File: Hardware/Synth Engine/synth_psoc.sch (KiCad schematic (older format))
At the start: 0 parts

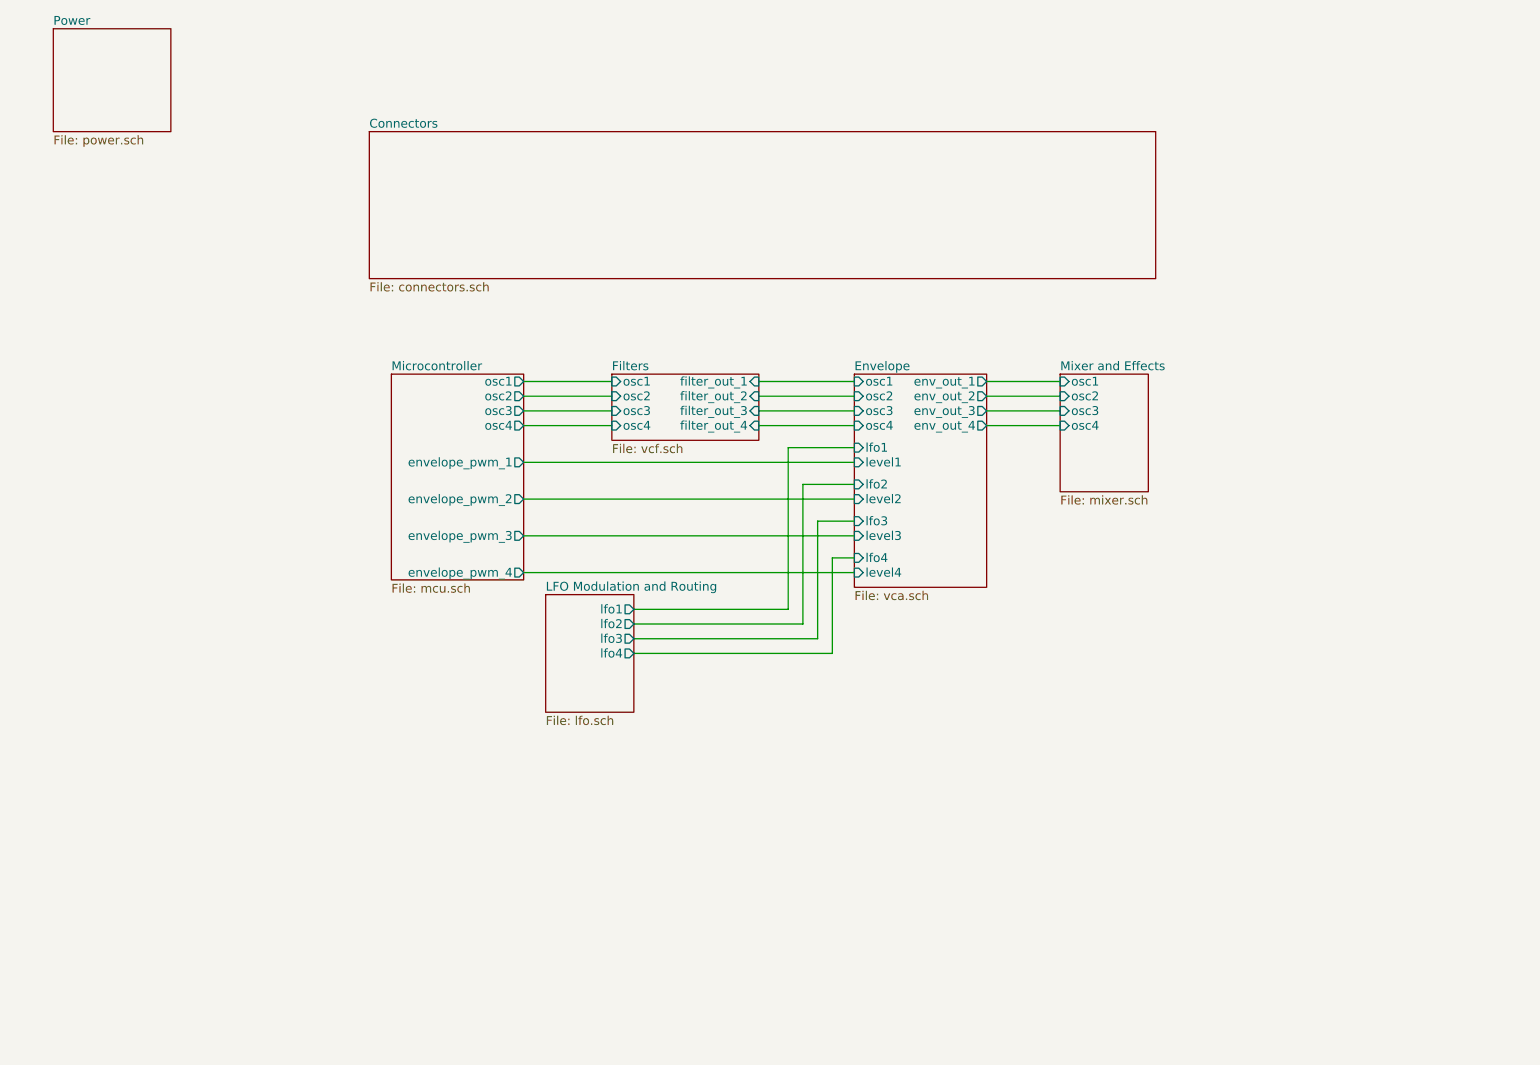
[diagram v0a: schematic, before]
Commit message: connect control board to main synth schem pages
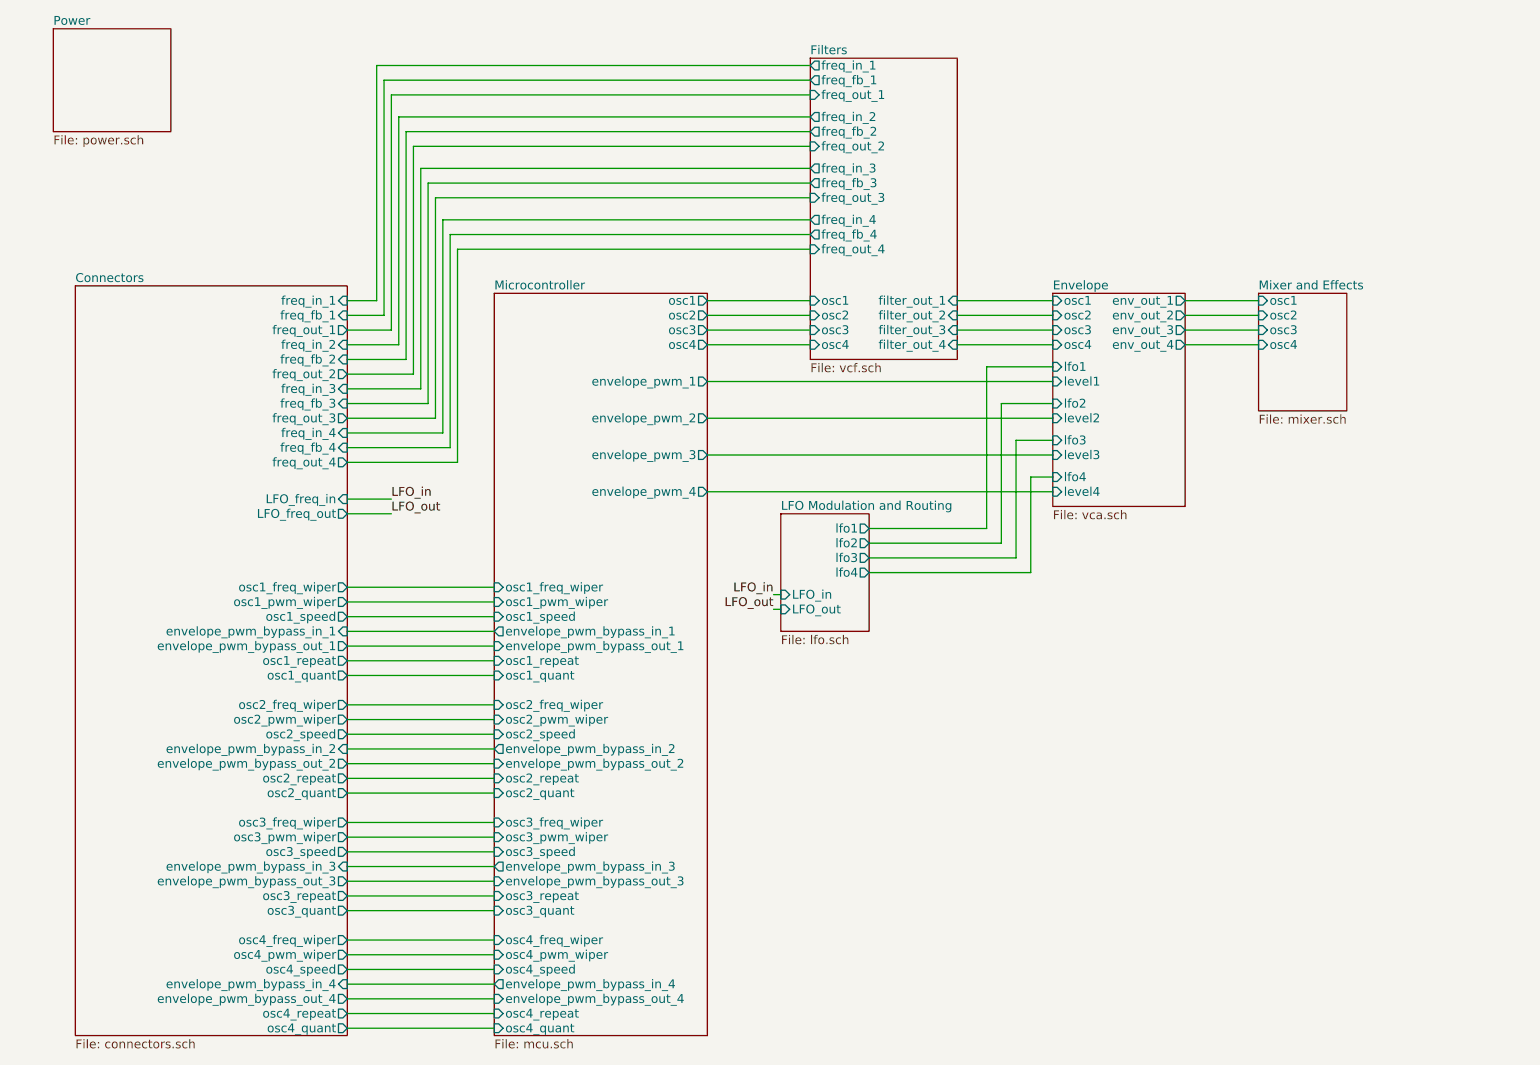
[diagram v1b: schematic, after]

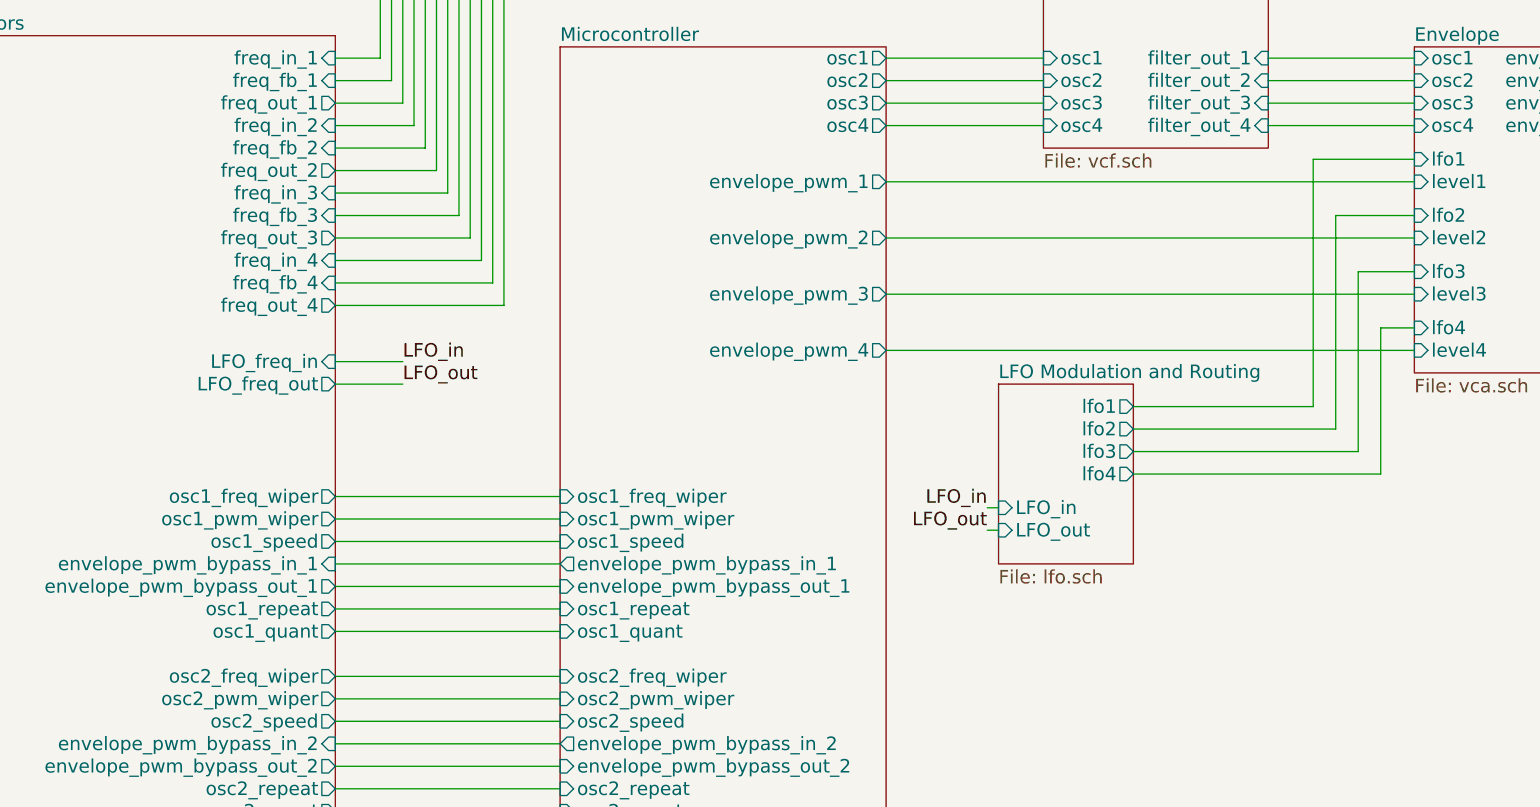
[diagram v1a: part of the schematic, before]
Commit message: remove extraneous net labels
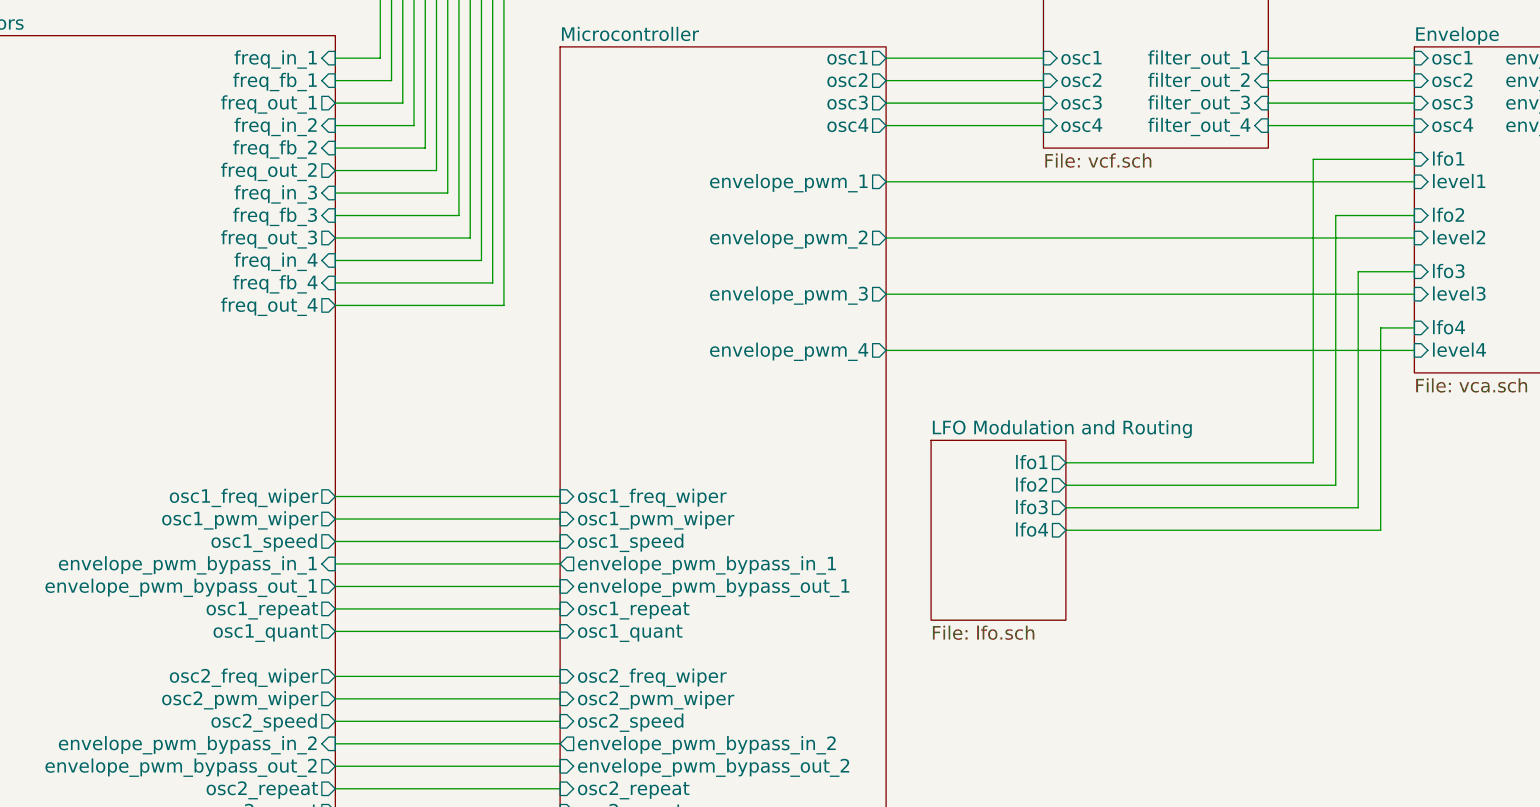
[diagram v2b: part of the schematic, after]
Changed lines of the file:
@@
 $EndSheet
 $Sheet
-S 5600 3950 600  800
+S 5300 4200 600  800
 U 5C35738C
 F0 "LFO Modulation and Routing" 60
 F1 "lfo.sch" 60
-F2 "lfo1" O R 6200 4050 60
-F3 "lfo2" O R 6200 4150 60
-F4 "lfo3" O R 6200 4250 60
-F5 "lfo4" O R 6200 4350 60
-F6 "LFO_in" I L 5600 4500 60
-F7 "LFO_out" I L 5600 4600 60
+F2 "lfo1" O R 5900 4300 60
+F3 "lfo2" O R 5900 4400 60
+F4 "lfo3" O R 5900 4500 60
+F5 "lfo4" O R 5900 4600 60
 $EndSheet
 $Sheet
@@
 F36 "osc4_repeat" O R 2650 7350 60
 F37 "osc4_quant" O R 2650 7450 60
-F38 "LFO_freq_in" I R 2650 3850 60
-F39 "LFO_freq_out" O R 2650 3950 60
-F40 "freq_fb_1" I R 2650 2600 60
-F41 "freq_fb_2" I R 2650 2900 60
-F42 "freq_fb_3" I R 2650 3200 60
-F43 "freq_fb_4" I R 2650 3500 60
+F38 "freq_fb_1" I R 2650 2600 60
+F39 "freq_fb_2" I R 2650 2900 60
+F40 "freq_fb_3" I R 2650 3200 60
+F41 "freq_fb_4" I R 2650 3500 60
 $EndSheet
 Wire Wire Line
@@
 	5100 3050 7450 3050
 Wire Wire Line
-	7300 4350 6200 4350
-Wire Wire Line
-	7300 3700 7300 4350
+	7300 4600 5900 4600
+Wire Wire Line
+	7300 3700 7300 4600
 Wire Wire Line
 	7450 3700 7300 3700
 Wire Wire Line
-	7200 4250 6200 4250
-Wire Wire Line
-	7200 3450 7200 4250
+	7200 4500 5900 4500
+Wire Wire Line
+	7200 3450 7200 4500
 Wire Wire Line
 	7450 3450 7200 3450
 Wire Wire Line
-	7100 4150 6200 4150
-Wire Wire Line
-	7100 3200 7100 4150
+	7100 4400 5900 4400
+Wire Wire Line
+	7100 3200 7100 4400
 Wire Wire Line
 	7450 3200 7100 3200
@@
 	7000 2950 7450 2950
 Wire Wire Line
-	7000 4050 7000 2950
-Wire Wire Line
-	6200 4050 7000 4050
+	7000 4300 7000 2950
+Wire Wire Line
+	5900 4300 7000 4300
 Wire Wire Line
 	8350 2800 8850 2800
@@
 Wire Wire Line
 	2650 7450 3650 7450
-Text Label 2950 3850 0    60   ~ 0
-LFO_in
-Text Label 2950 3950 0    60   ~ 0
-LFO_out
-Wire Wire Line
-	2950 3850 2650 3850
-Wire Wire Line
-	2650 3950 2950 3950
-Text Label 5550 4500 2    60   ~ 0
-LFO_in
-Text Label 5550 4600 2    60   ~ 0
-LFO_out
-Wire Wire Line
-	5550 4500 5600 4500
-Wire Wire Line
-	5550 4600 5600 4600
 $EndSCHEMATC

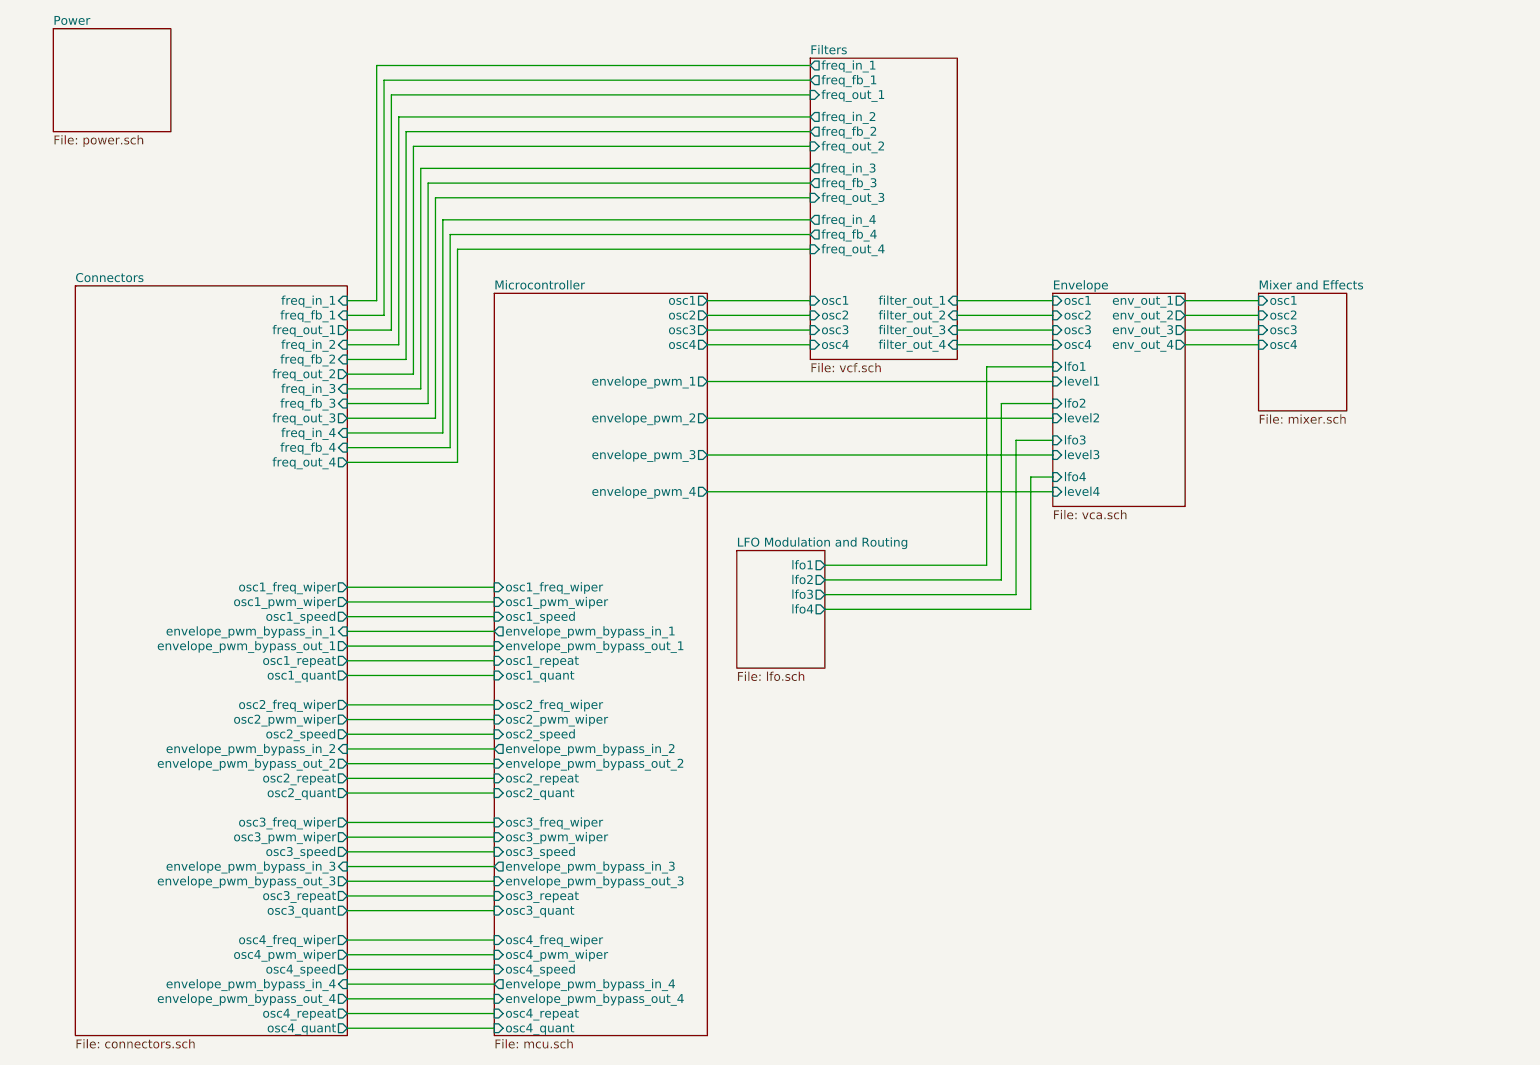
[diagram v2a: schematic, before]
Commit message: fix LFO connector schem
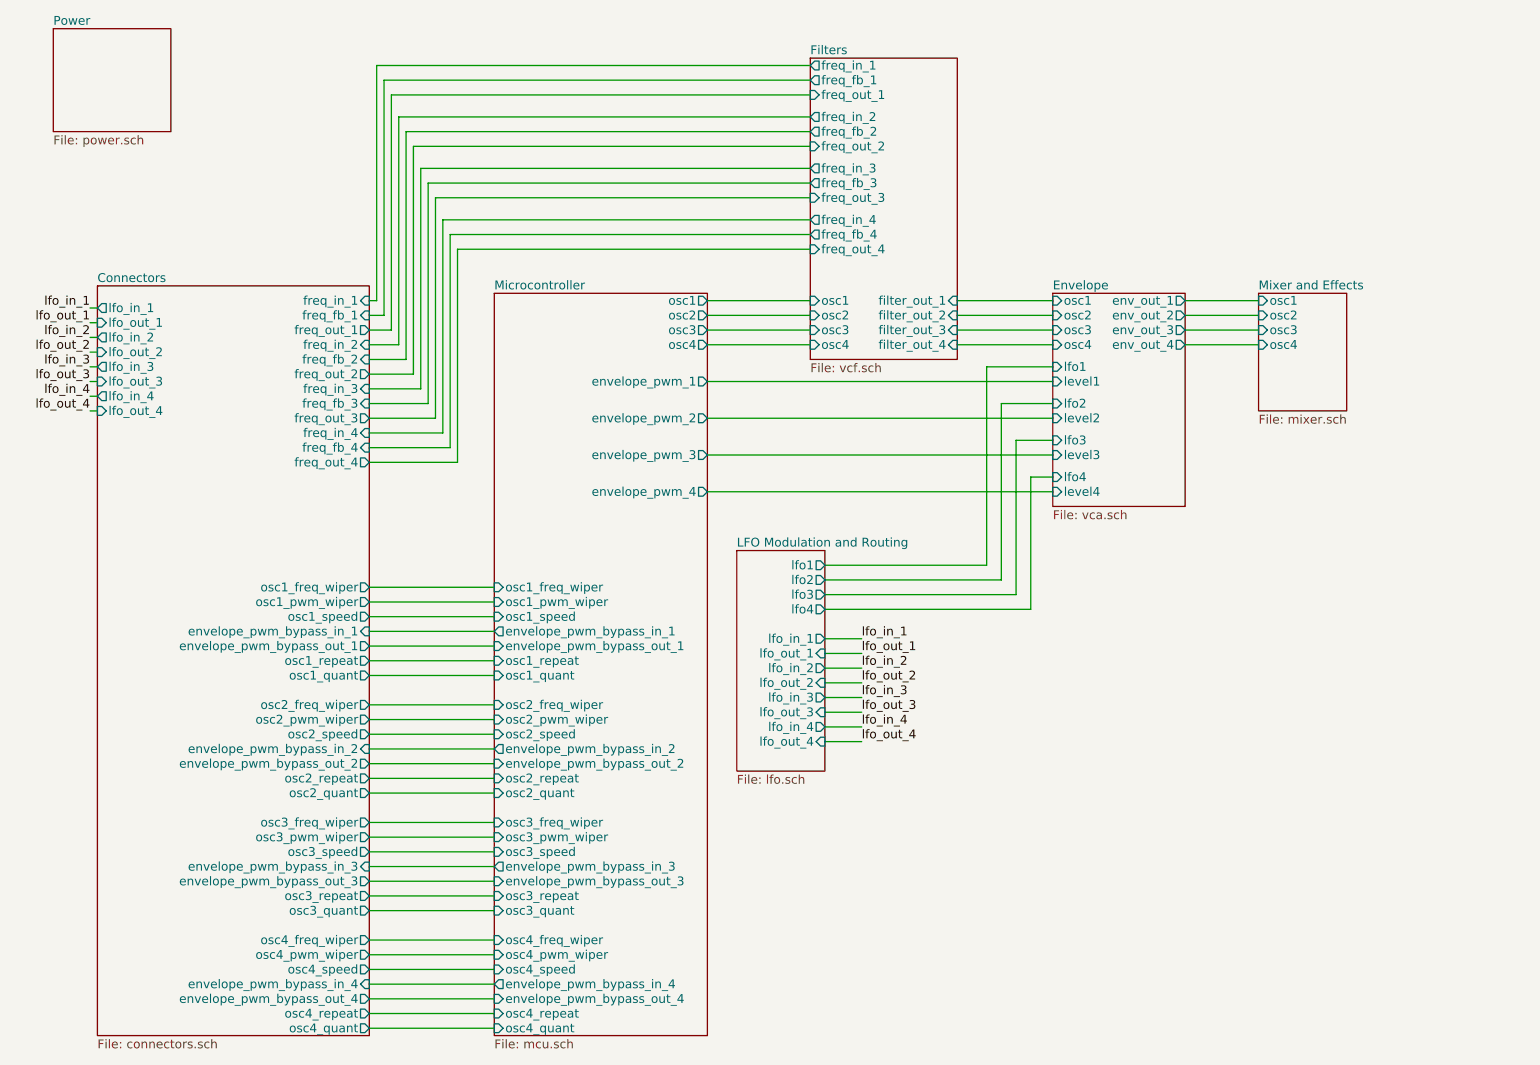
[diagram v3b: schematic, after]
